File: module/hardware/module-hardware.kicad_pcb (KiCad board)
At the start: 4 copper layers, 74 parts, among them J1 USB_B_Micro, J10 Conn_01x03, J11 Conn_01x03, J12 Conn_01x03, J2 40Pin 0.1", J3 Conn_01x02_Male, J4 40Pin 0.1", J5 Conn_01x03_Male, J6 Conn_01x03_Male, J7 Conn_01x03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

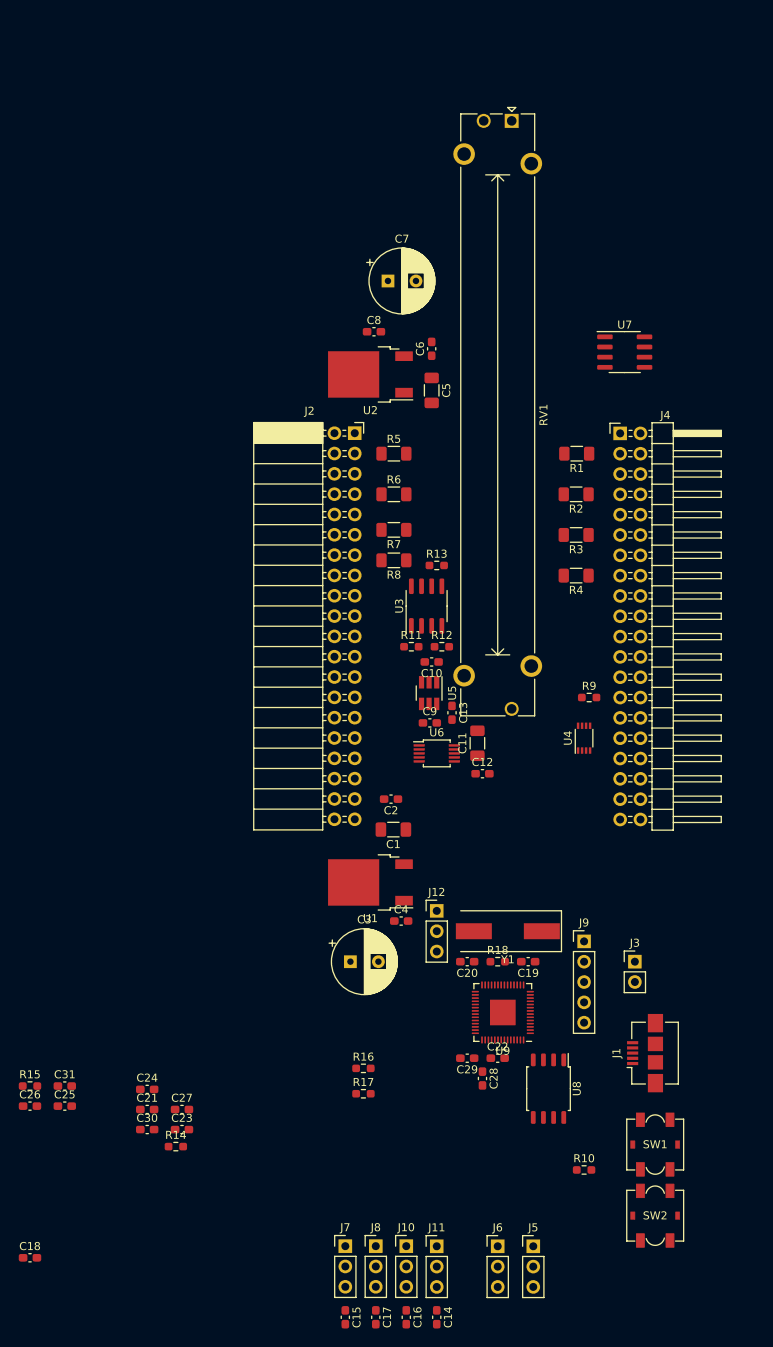
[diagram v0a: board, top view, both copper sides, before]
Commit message: Complete board layout component placement & outline approx
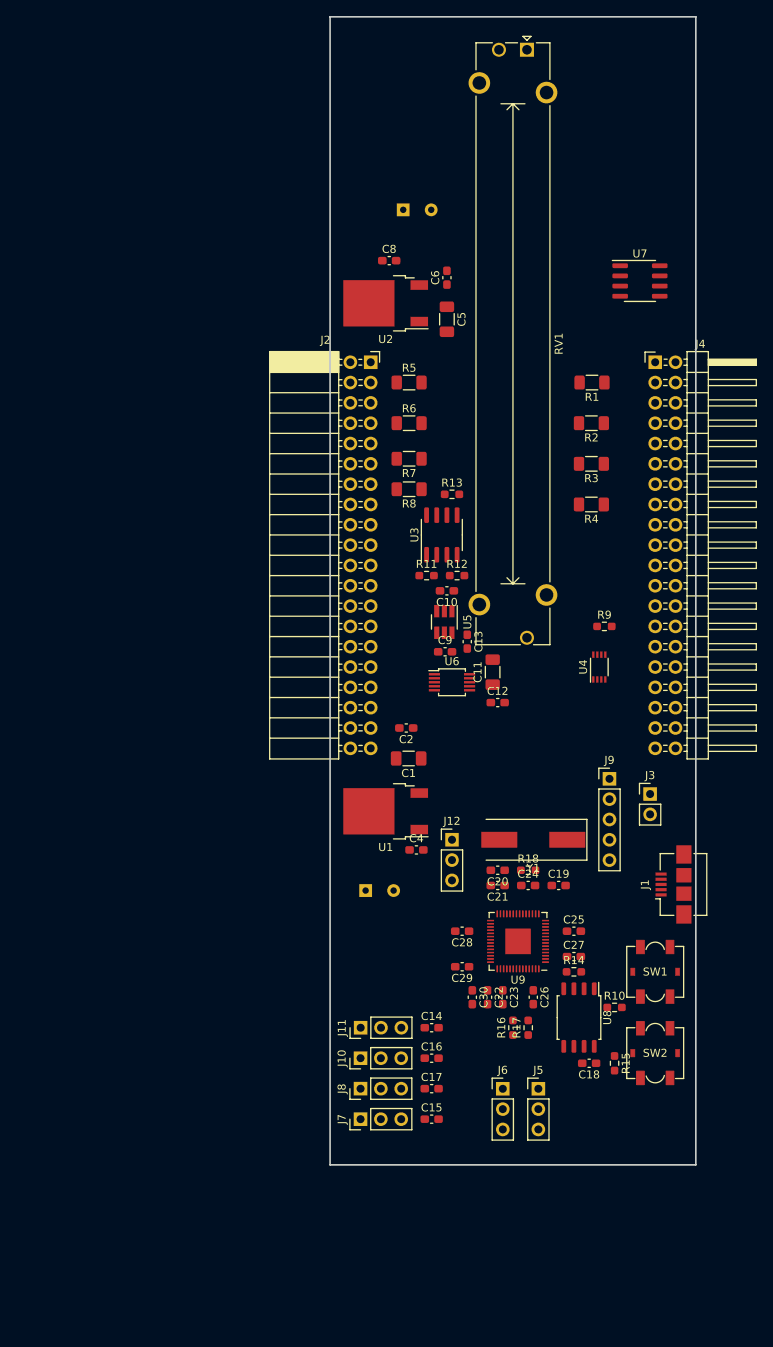
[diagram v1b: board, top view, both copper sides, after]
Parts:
- removed C31: 1u, Capacitor_SMD:C_0603_1608Metric_Pad1.08x0.95mm_HandSolder
- C3, C7: moved to B.Cu
- C30: value 0.1u -> 1u
- moved C18 74.0 mm to (155.6, 154.9), turned to 180 degrees
- moved R15 73.1 mm to (158.8, 154.9), turned to -90 degrees
- moved C25 67.3 mm to (153.7, 138.4)
- moved C26 64.4 mm to (148.6, 146.7), turned to -90 degrees
- moved R14 54.3 mm to (153.7, 143.5)
- moved C24 54.0 mm to (148.0, 132.7)
- moved C27 52.6 mm to (153.7, 141.6)
- moved C21 52.0 mm to (144.1, 132.7), turned to 180 degrees
- moved C30 43.9 mm to (141.0, 146.7), turned to -90 degrees
- moved C23 43.4 mm to (144.8, 146.7), turned to -90 degrees
- moved C14 36.2 mm to (135.9, 150.5), turned to 0 degrees
- moved C16 32.5 mm to (135.9, 154.3), turned to 0 degrees
- moved C17 29.4 mm to (135.9, 158.1), turned to 0 degrees
- moved J11 28.9 mm to (127.0, 150.5), turned to 90 degrees
- moved C15 27.0 mm to (135.9, 161.9), turned to 0 degrees
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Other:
- board outline added: 45.7 x 143.5 mm

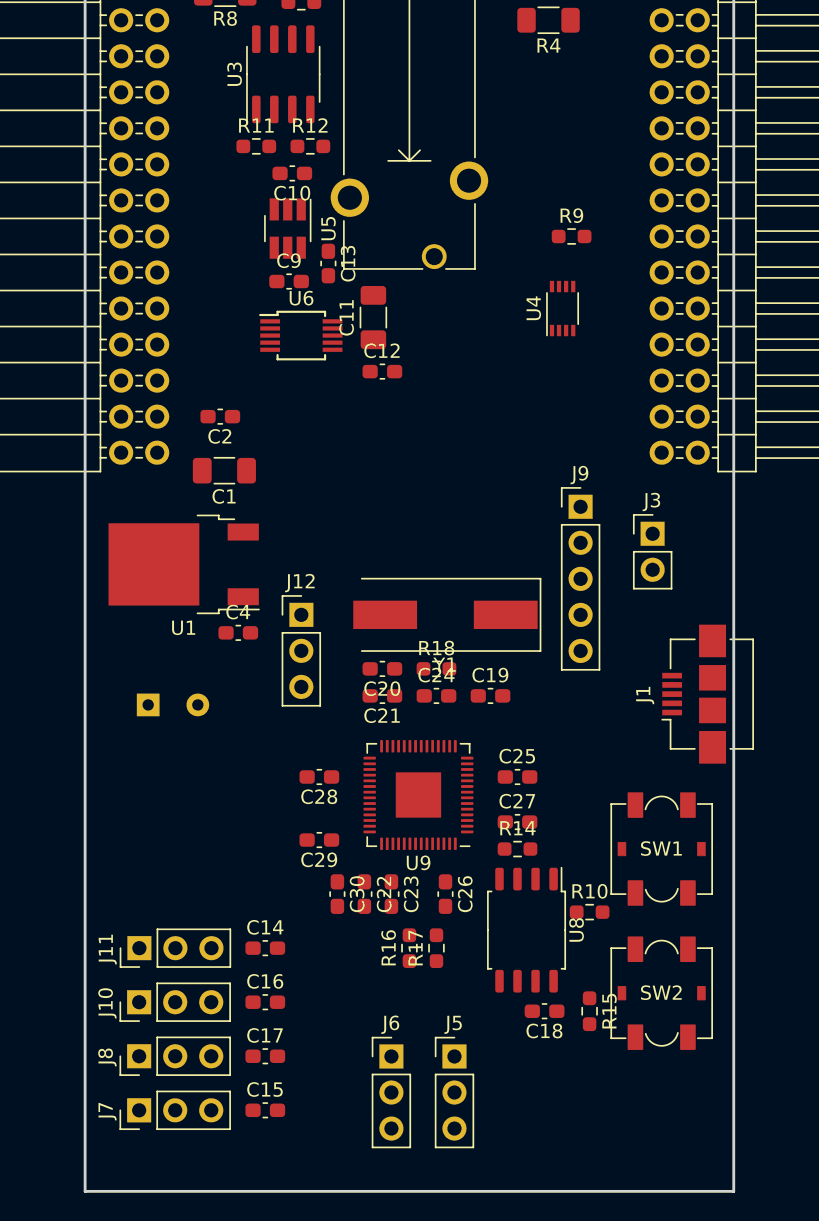
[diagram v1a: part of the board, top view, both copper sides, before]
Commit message: Begin digital side routing
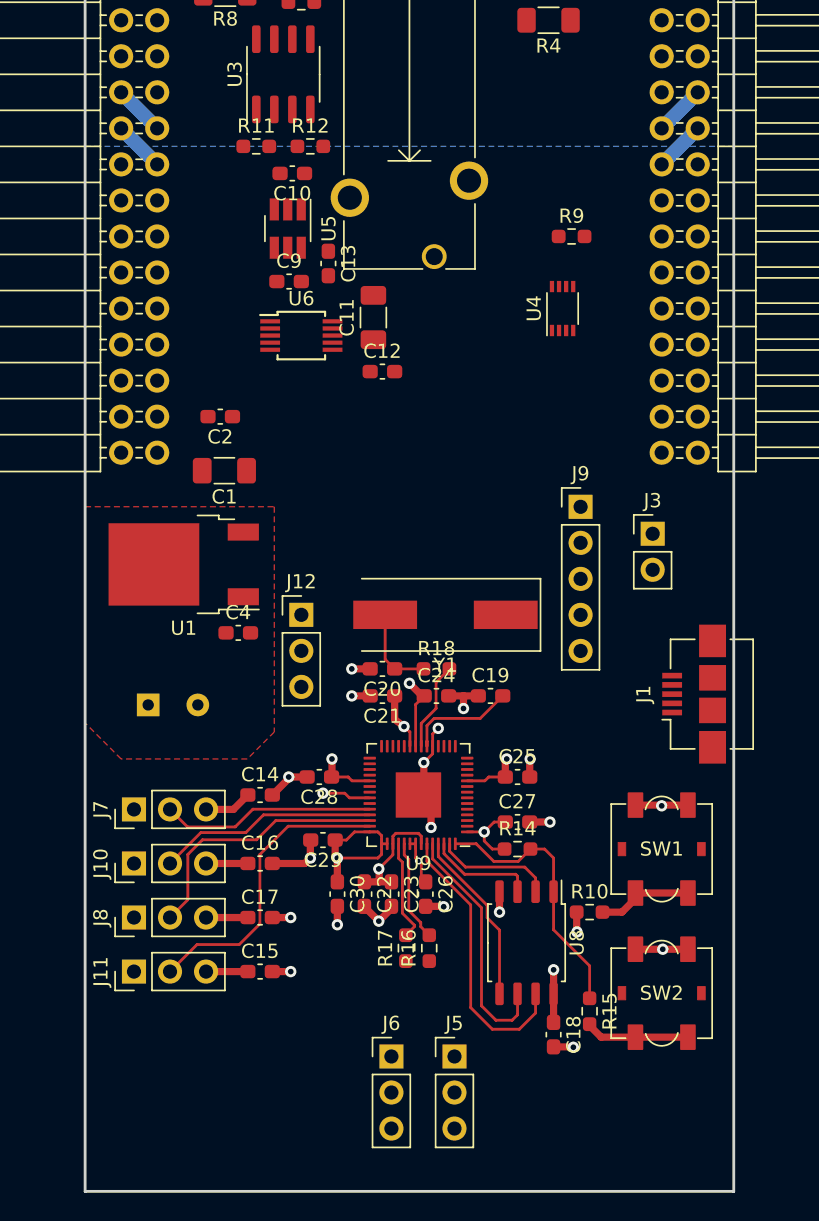
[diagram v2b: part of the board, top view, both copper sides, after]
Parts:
- moved J7 21.2 mm to (126.6, 140.7)
- moved C14 10.8 mm to (135.5, 139.7)
- moved C15 9.79 mm to (135.5, 152.1)
- moved C16 9.79 mm to (135.5, 144.5)
- moved C17 9.79 mm to (135.5, 148.3)
- moved J10 9.79 mm to (126.6, 144.5)
- moved J8 9.79 mm to (126.6, 148.3)
- moved R17 2.16 mm to (145.8, 150.5)
- moved C18 1.77 mm to (156.2, 156.6), turned to -90 degrees
- moved J11 1.69 mm to (126.6, 152.1)
- moved C26 1.40 mm to (147.2, 146.7)
- moved R16 1.40 mm to (147.4, 150.5)
- moved U8 0.89 mm to (154.3, 150.1)
- moved C29 0.25 mm to (140.0, 142.9)
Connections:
- net Net-(R16-Pad2) renamed /D.R.U.M. Module Digital/_USB_D+
- net Net-(R17-Pad2) renamed /D.R.U.M. Module Digital/_USB_D-
- U9 pad 35: unconnected-(U9-Pad35) -> /D.R.U.M. Module Digital/GPIO4_BTN0
- U9 pad 36: unconnected-(U9-Pad36) -> /D.R.U.M. Module Digital/GPIO5_BTN1
- U9 pad 6: /D.R.U.M. Module Digital/GPIO4_BTN0 -> unconnected-(U9-Pad6)
- U9 pad 7: /D.R.U.M. Module Digital/GPIO5_BTN1 -> unconnected-(U9-Pad7)
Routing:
- net +3V3: track 0.00 -> 52.8 mm, vias 0 -> 8
- net GND: track 0.00 -> 49.0 mm, vias 0 -> 19
- net /D.R.U.M. Module Digital/GPIO5_BTN1: track 0.00 -> 26.5 mm, vias 0 -> 1
- net /D.R.U.M. Module Digital/GPIO29_ADC3: track 0.00 -> 21.2 mm
- net /D.R.U.M. Module Digital/FD3: track 0.00 -> 19.9 mm
- net /D.R.U.M. Module Digital/FCSB: track 0.00 -> 19.0 mm
- net /D.R.U.M. Module Digital/GPIO28_ADC2: track 0.00 -> 18.8 mm
- net /D.R.U.M. Module Digital/FSCLK: track 0.00 -> 17.4 mm
- net /D.R.U.M. Module Digital/GPIO27_ADC1: track 0.00 -> 15.5 mm
- net /D.R.U.M. Module Digital/GPIO26_ADC0: track 0.00 -> 15.1 mm
- net /D.R.U.M. Module Digital/FD0: track 0.00 -> 12.4 mm
- net +1V1: track 0.00 -> 12.3 mm, vias 0 -> 2
- net /D.R.U.M. Module Digital/FD1: track 0.00 -> 8.33 mm
- net Net-(C19-Pad2): track 0.00 -> 8.00 mm
- net /D.R.U.M. Module Digital/FD2: track 0.00 -> 7.64 mm
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- added copper zone on In2.Cu, net +1V1
- added copper zone on F.Cu, net +3V3
- added copper zone on In1.Cu, net +3V3
- added copper zone on B.Cu, net GND

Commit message: Ground plane
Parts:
- added R19: 10k, Resistor_SMD:R_0603_1608Metric_Pad0.98x0.95mm_HandSolder, F.Cu at (152.0, 161.9)
- added R20: 10k, Resistor_SMD:R_0603_1608Metric_Pad0.98x0.95mm_HandSolder, F.Cu at (142.0, 161.9)
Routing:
- added copper zone on B.Cu, net GNDA
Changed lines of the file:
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@@
     )
   )
+  (footprint "Resistor_SMD:R_0603_1608Metric_Pad0.98x0.95mm_HandSolder" (layer "F.Cu")
+    (at 141.986 161.925 -90)
+    (descr "Resistor SMD 0603 (1608 Metric), square (rectangular) end terminal, IPC_7351 nominal with elongated pad for handsoldering. (Body size source: IPC-SM-782 page 72, https://www.pcb-3d.com/wordpress/wp-content/uploads/ipc-sm-782a_amendment_1_and_2.pdf), generated with kicad-footprint-generator")
+    (tags "resistor handsolder")
+    (property "Sheetfile" "digital.kicad_sch")
+    (property "Sheetname" "D.R.U.M. Module Digital")
+    (attr smd)
+    (fp_text reference "R20" (at 0 -1.43 90) (layer "F.SilkS")
+      (effects (font (size 1 1) (thickness 0.15)))
+    )
+    (fp_text value "10k" (at 0 1.43 90) (layer "F.Fab")
+      (effects (font (size 1 1) (thickness 0.15)))
+    )
+    (fp_text user "${REFERENCE}" (at 0 0 90) (layer "F.Fab")
+      (effects (font (size 0.4 0.4) (thickness 0.06)))
+    )
+    (fp_line (start -0.254724 -0.5225) (end 0.254724 -0.5225) (layer "F.SilkS") (width 0.12))
+    (fp_line (start -0.254724 0.5225) (end 0.254724 0.5225) (layer "F.SilkS") (width 0.12))
+    (fp_line (start -1.65 0.73) (end -1.65 -0.73) (layer "F.CrtYd") (width 0.05))
+    (fp_line (start 1.65 0.73) (end -1.65 0.73) (layer "F.CrtYd") (width 0.05))
+    (fp_line (start 1.65 -0.73) (end 1.65 0.73) (layer "F.CrtYd") (width 0.05))
+    (fp_line (start -1.65 -0.73) (end 1.65 -0.73) (layer "F.CrtYd") (width 0.05))
+    (fp_line (start -0.8 -0.4125) (end 0.8 -0.4125) (layer "F.Fab") (width 0.1))
+    (fp_line (start 0.8 0.4125) (end -0.8 0.4125) (layer "F.Fab") (width 0.1))
+    (fp_line (start -0.8 0.4125) (end -0.8 -0.4125) (layer "F.Fab") (width 0.1))
+    (fp_line (start 0.8 -0.4125) (end 0.8 0.4125) (layer "F.Fab") (width 0.1))
+    (pad "1" smd roundrect (at -0.9125 0 270) (size 0.975 0.95) (layers "F.Cu" "F.Paste" "F.Mask") (roundrect_rratio 0.25)
+      (net 36 "/D.R.U.M. Module Digital/GPIO5_BTN1") (pintype "passive"))
+    (pad "2" smd roundrect (at 0.9125 0 270) (size 0.975 0.95) (layers "F.Cu" "F.Paste" "F.Mask") (roundrect_rratio 0.25)
+      (net 3 "+3V3") (pintype "passive"))
+    (model "${KICAD6_3DMODEL_DIR}/Resistor_SMD.3dshapes/R_0603_1608Metric.wrl"
+      (offset (xyz 0 0 0))
+      (scale (xyz 1 1 1))
+      (rotate (xyz 0 0 0))
+    )
+  )
   (footprint "Capacitor_SMD:C_0603_1608Metric_Pad1.08x0.95mm_HandSolder" (layer "F.Cu")
     (at 139.954 142.875 180)
@@
     )
   )
+  (footprint "Resistor_SMD:R_0603_1608Metric_Pad0.98x0.95mm_HandSolder" (layer "F.Cu")
+    (at 152.019 161.925 -90)
+    (descr "Resistor SMD 0603 (1608 Metric), square (rectangular) end terminal, IPC_7351 nominal with elongated pad for handsoldering. (Body size source: IPC-SM-782 page 72, https://www.pcb-3d.com/wordpress/wp-content/uploads/ipc-sm-782a_amendment_1_and_2.pdf), generated with kicad-footprint-generator")
+    (tags "resistor handsolder")
+    (property "Sheetfile" "digital.kicad_sch")
+    (property "Sheetname" "D.R.U.M. Module Digital")
+    (attr smd)
+    (fp_text reference "R19" (at 0 -1.43 90) (layer "F.SilkS")
+      (effects (font (size 1 1) (thickness 0.15)))
+    )
+    (fp_text value "10k" (at 0 1.43 90) (layer "F.Fab")
+      (effects (font (size 1 1) (thickness 0.15)))
+    )
+    (fp_text user "${REFERENCE}" (at 0 0 90) (layer "F.Fab")
+      (effects (font (size 0.4 0.4) (thickness 0.06)))
+    )
+    (fp_line (start -0.254724 -0.5225) (end 0.254724 -0.5225) (layer "F.SilkS") (width 0.12))
+    (fp_line (start -0.254724 0.5225) (end 0.254724 0.5225) (layer "F.SilkS") (width 0.12))
+    (fp_line (start 1.65 0.73) (end -1.65 0.73) (layer "F.CrtYd") (width 0.05))
+    (fp_line (start -1.65 0.73) (end -1.65 -0.73) (layer "F.CrtYd") (width 0.05))
+    (fp_line (start -1.65 -0.73) (end 1.65 -0.73) (layer "F.CrtYd") (width 0.05))
+    (fp_line (start 1.65 -0.73) (end 1.65 0.73) (layer "F.CrtYd") (width 0.05))
+    (fp_line (start 0.8 0.4125) (end -0.8 0.4125) (layer "F.Fab") (width 0.1))
+    (fp_line (start -0.8 0.4125) (end -0.8 -0.4125) (layer "F.Fab") (width 0.1))
+    (fp_line (start -0.8 -0.4125) (end 0.8 -0.4125) (layer "F.Fab") (width 0.1))
+    (fp_line (start 0.8 -0.4125) (end 0.8 0.4125) (layer "F.Fab") (width 0.1))
+    (pad "1" smd roundrect (at -0.9125 0 270) (size 0.975 0.95) (layers "F.Cu" "F.Paste" "F.Mask") (roundrect_rratio 0.25)
+      (net 35 "/D.R.U.M. Module Digital/GPIO4_BTN0") (pintype "passive"))
+    (pad "2" smd roundrect (at 0.9125 0 270) (size 0.975 0.95) (layers "F.Cu" "F.Paste" "F.Mask") (roundrect_rratio 0.25)
+      (net 3 "+3V3") (pintype "passive"))
+    (model "${KICAD6_3DMODEL_DIR}/Resistor_SMD.3dshapes/R_0603_1608Metric.wrl"
+      (offset (xyz 0 0 0))
+      (scale (xyz 1 1 1))
+      (rotate (xyz 0 0 0))
+    )
+  )
   (footprint "Capacitor_SMD:C_0603_1608Metric_Pad1.08x0.95mm_HandSolder" (layer "F.Cu")
     (at 144.78 146.685 -90)
@@
     )
   )
+  (zone (net 5) (net_name "GNDA") (layer "B.Cu") (hatch edge 0.508)
+    (connect_pads yes (clearance 0.508))
+    (min_thickness 0.254) (filled_areas_thickness no)
+    (fill yes (thermal_gap 0.508) (thermal_bridge_width 0.508))
+    (polygon
+      (pts
+        (xy 168.91 91.44)
+        (xy 123.19 91.44)
+        (xy 123.19 24.13)
+        (xy 168.91 24.13)
+      )
+    )
+  )
   (zone (net 2) (net_name "GND") (layer "B.Cu") (hatch edge 0.508)
-    (connect_pads (clearance 0.508))
+    (connect_pads yes (clearance 0.508))
     (min_thickness 0.254) (filled_areas_thickness no)
     (fill yes (thermal_gap 0.508) (thermal_bridge_width 0.508))

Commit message: Route/move USB
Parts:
- moved J3 50.7 mm to (126.6, 156.3)
- moved J1 47.0 mm to (132.0, 164.8), turned to 0 degrees
- moved J9 8.36 mm to (163.7, 125.6)
- moved R19 1.77 mm to (153.7, 161.3)
- moved R20 1.20 mm to (141.0, 161.3)
- moved R16 0.77 mm to (146.7, 150.6)
- moved R17 0.77 mm to (145.0, 150.6)
- moved J5 0.64 mm to (149.9, 158.1)
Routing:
- net /RUN: track 6.81 -> 41.8 mm, vias 0 -> 2
- net /D.R.U.M. Module Digital/GPIO4_BTN0: track 0.00 -> 32.8 mm, vias 0 -> 1
- net GND: track 49.0 -> 75.4 mm, vias 19 -> 22
- net /USB_D-: track 0.00 -> 22.9 mm
- net /USB_D+: track 0.00 -> 22.9 mm
- net /D.R.U.M. Module Digital/GPIO3_ENC2: track 0.00 -> 21.0 mm
- net /D.R.U.M. Module Digital/GPIO2_ENC1: track 0.00 -> 19.0 mm
- net /D.R.U.M. Module Digital/GPIO1_ENC0: track 0.00 -> 17.0 mm
- net Net-(J12-Pad1): track 0.00 -> 13.8 mm
- net Net-(J12-Pad3): track 0.00 -> 9.06 mm
- net +3V3: track 52.8 -> 59.6 mm
- net Net-(J1-Pad1): track 0.00 -> 6.39 mm
- net /D.R.U.M. Module Digital/GPIO5_BTN1: track 26.5 -> 32.6 mm
- net Net-(C19-Pad2): track 8.00 -> 13.5 mm
- added copper zone on B.Cu, net +3V3
- added copper zone on In1.Cu, net GND
- removed copper zone on In1.Cu, net +3V3
- removed copper zone on B.Cu, net GND
